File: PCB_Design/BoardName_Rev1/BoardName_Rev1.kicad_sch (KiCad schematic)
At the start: 0 parts

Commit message: Added Initial Schematic with an Example Hierarchical Sheet
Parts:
- added H1, H2, H3, H4: MountingHole, MountingHole:MountingHole_3.2mm_M3_ISO7380_Pad_TopBottom, symbol Mechanical:MountingHole
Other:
- added sheet Power_Section (Schematic/Power_Section.kicad_sch)
- note added: "16CH"
- note added: "BLOCK DIAGRAM"
- note added: "BoardName"
- note added: "Buzzer Support"
- note added: "GPIO Expander 0 (8CH)"
- note added: "GPIO Expander 1 (8CH)"
- note added: "I2C CH0"
- note added: "I2C CH1"
- note added: "LED 0"
- note added: "LED 7"
- note added: "Main Board Status LED (Debug)"
- note added: "Main Component Selection"
- note added: "Olimex ESP32 PoE Board"
- note added: "PN531 0"
- note added: "PN531 1"
- note added: "PN531 7"
- note added: "SW 0"
- note added: "SW 1"
- note added: "SW 7"
- note added: "UART Expander 0-1 (4CH * 2) / SPI Expander 0 (16CH / 2)"
- note added: "UART Expander 2-3 (4CH * 2) / SPI Expander 0 (16CH / 2)"
- note added: "Upload Program Port (UART)"
- company: (none) -> Elementz Engineers Guild
- title: (none) -> BoardName

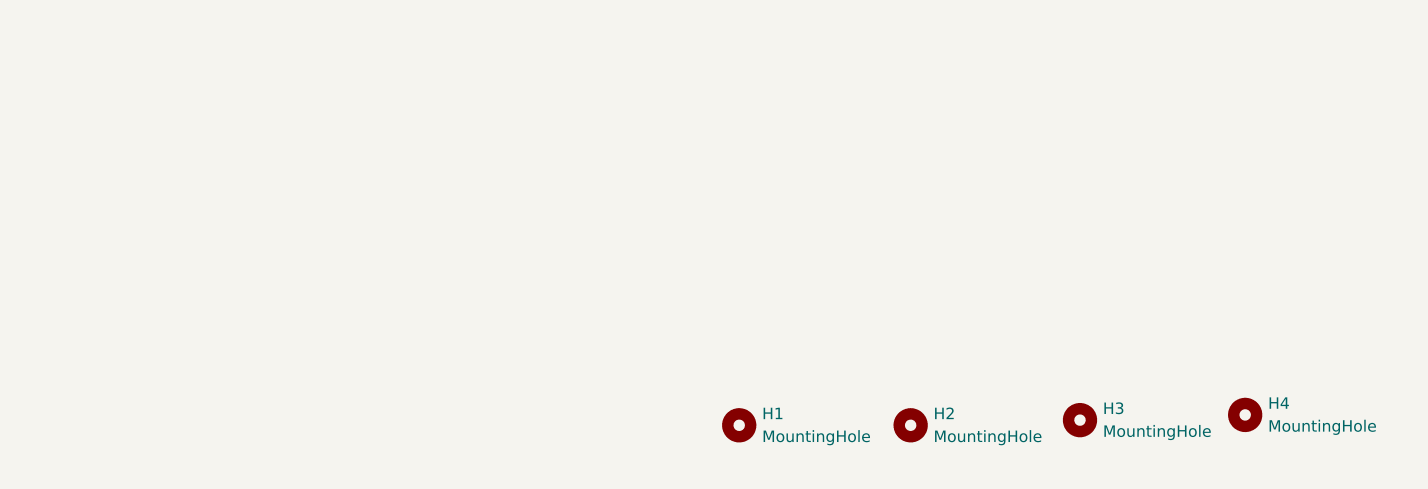
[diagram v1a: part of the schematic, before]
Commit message: Improved PCB Design Example Template
- Setup Board Constraints (Based on JLC04161H-7628)
- Default Symbol & Footprint Library (Small Shield Clips Added)
- Added Board Info on PCB Design Page
- Added Additional Texts in User Comments as Additional Docs
- Updated .gitignore
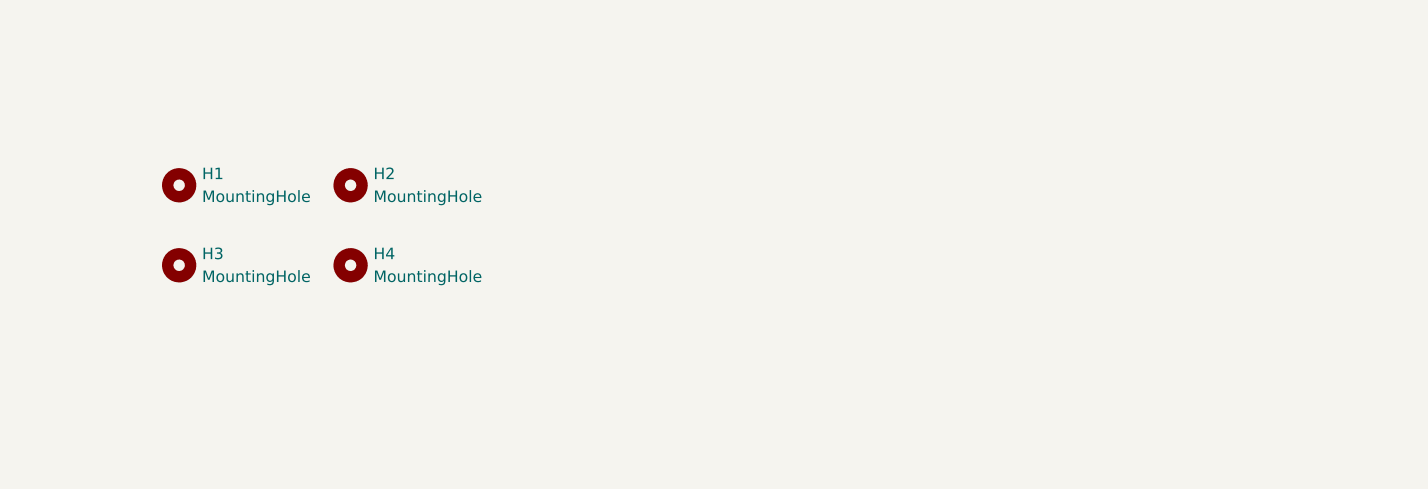
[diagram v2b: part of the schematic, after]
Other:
- moved on the sheet: H1, H2, H3, H4
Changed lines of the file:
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@@
 	(generator "eeschema")
 	(generator_version "9.0")
-	(paper "A3")
+	(paper "A4")
 	(title_block
 		(title "BoardName")
-		(date "2025-06-02")
+		(date "2026-04-06")
 		(rev "Rev1")
 		(company "Elementz Engineers Guild")
@@
 	(symbol
 		(lib_id "Mechanical:MountingHole")
-		(at 355.9388 158.8687 0)
+		(at 256.54 142.24 0)
 		(unit 1)
 		(exclude_from_sim no)
@@
 		(fields_autoplaced yes)
 		(property "Reference" "H4"
-			(at 358.4788 157.5986 0)
+			(at 259.08 140.9699 0)
 			(effects
 				(font
@@
 		)
 		(property "Value" "MountingHole"
-			(at 358.4788 160.1386 0)
+			(at 259.08 143.5099 0)
 			(effects
 				(font
@@
 		)
 		(property "Footprint" "MountingHole:MountingHole_3.2mm_M3_ISO7380_Pad_TopBottom"
-			(at 355.9388 158.8687 0)
+			(at 256.54 142.24 0)
 			(effects
 				(font
@@
 		)
 		(property "Datasheet" "~"
-			(at 355.9388 158.8687 0)
+			(at 256.54 142.24 0)
 			(effects
 				(font
@@
 		)
 		(property "Description" "Mounting Hole without connection"
-			(at 355.9388 158.8687 0)
+			(at 256.54 142.24 0)
 			(effects
 				(font
@@
 	(symbol
 		(lib_id "Mechanical:MountingHole")
-		(at 318.77 160.02 0)
+		(at 256.54 133.35 0)
 		(unit 1)
 		(exclude_from_sim no)
@@
 		(fields_autoplaced yes)
 		(property "Reference" "H2"
-			(at 321.31 158.7499 0)
+			(at 259.08 132.0799 0)
 			(effects
 				(font
@@
 		)
 		(property "Value" "MountingHole"
-			(at 321.31 161.2899 0)
+			(at 259.08 134.6199 0)
 			(effects
 				(font
@@
 		)
 		(property "Footprint" "MountingHole:MountingHole_3.2mm_M3_ISO7380_Pad_TopBottom"
-			(at 318.77 160.02 0)
+			(at 256.54 133.35 0)
 			(effects
 				(font
@@
 		)
 		(property "Datasheet" "~"
-			(at 318.77 160.02 0)
+			(at 256.54 133.35 0)
 			(effects
 				(font
@@
 		)
 		(property "Description" "Mounting Hole without connection"
-			(at 318.77 160.02 0)
+			(at 256.54 133.35 0)
 			(effects
 				(font
@@
 	(symbol
 		(lib_id "Mechanical:MountingHole")
-		(at 337.5852 159.4459 0)
+		(at 237.49 142.24 0)
 		(unit 1)
 		(exclude_from_sim no)
@@
 		(fields_autoplaced yes)
 		(property "Reference" "H3"
-			(at 340.1252 158.1758 0)
+			(at 240.03 140.9699 0)
 			(effects
 				(font
@@
 		)
 		(property "Value" "MountingHole"
-			(at 340.1252 160.7158 0)
+			(at 240.03 143.5099 0)
 			(effects
 				(font
@@
 		)
 		(property "Footprint" "MountingHole:MountingHole_3.2mm_M3_ISO7380_Pad_TopBottom"
-			(at 337.5852 159.4459 0)
+			(at 237.49 142.24 0)
 			(effects
 				(font
@@
 		)
 		(property "Datasheet" "~"
-			(at 337.5852 159.4459 0)
+			(at 237.49 142.24 0)
 			(effects
 				(font
@@
 		)
 		(property "Description" "Mounting Hole without connection"
-			(at 337.5852 159.4459 0)
+			(at 237.49 142.24 0)
 			(effects
 				(font
@@
 	(symbol
 		(lib_id "Mechanical:MountingHole")
-		(at 299.72 160.02 0)
+		(at 237.49 133.35 0)
 		(unit 1)
 		(exclude_from_sim no)
@@
 		(fields_autoplaced yes)
 		(property "Reference" "H1"
-			(at 302.26 158.7499 0)
+			(at 240.03 132.0799 0)
 			(effects
 				(font
@@
 		)
 		(property "Value" "MountingHole"
-			(at 302.26 161.2899 0)
+			(at 240.03 134.6199 0)
 			(effects
 				(font
@@
 		)
 		(property "Footprint" "MountingHole:MountingHole_3.2mm_M3_ISO7380_Pad_TopBottom"
-			(at 299.72 160.02 0)
+			(at 237.49 133.35 0)
 			(effects
 				(font
@@
 		)
 		(property "Datasheet" "~"
-			(at 299.72 160.02 0)
+			(at 237.49 133.35 0)
 			(effects
 				(font
@@
 		)
 		(property "Description" "Mounting Hole without connection"
-			(at 299.72 160.02 0)
-			(effects
-				(font
+			(at 237.49 133.35 0)
+			(effects
+				(font
